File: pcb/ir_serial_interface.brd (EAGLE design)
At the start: 41.6 x 43.2 mm, 24 parts, among them IC1 PIC18F2550_28W, Q1 BSS123, T1 SFH303

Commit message: PCB: board layout done
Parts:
- removed GND, LEFT, MIC, RIGHT: LSP10, solpad:LSP10
- removed Q1: BSS123, transistor-small-signal:SOT23
- added D2: (no value), semicon-smd-ipc:SOT23
- added IC2: LP2992, texas:SOT23-DBV
- added Q2: BC847SMD, transistor-npn:SOT23
- added R10: 2k, resistor:M0805
- added R11, R12, R13: 100k, resistor:M0805
- added U$2: AUDIO-JACK3, SparkFun-Connectors:AUDIO-JACK-TRRS-SMD
- moved R3 23.3 mm to (53.3, 27.9), turned to 0 degrees
- moved C4 23.3 mm to (50.8, 47.0), turned to 0 degrees
- moved R9 19.1 mm to (25.4, 46.4), turned to 180 degrees
- moved C1 18.9 mm to (52.4, 30.8), turned to 0 degrees
- moved R4 17.6 mm to (48.9, 27.9), turned to 0 degrees
- moved U$1 17.4 mm to (42.5, 47.6)
- moved D4 16.7 mm to (24.1, 41.9), turned to 270 degrees
- moved T1 16.7 mm to (24.1, 34.3)
- moved R1 16.5 mm to (35.6, 47.6), turned to 0 degrees
- moved BAT1 15.9 mm to (46.4, 38.1)
- moved R2 15.3 mm to (25.4, 29.2), turned to 180 degrees
- moved D1 14.8 mm to (27.9, 41.9), turned to 270 degrees
- moved R8 11.0 mm to (29.8, 46.4), turned to 180 degrees
- moved R7 10.8 mm to (50.8, 43.8), turned to 180 degrees
- moved C2 7.62 mm to (44.5, 27.9), turned to 180 degrees
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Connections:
- removed net -: BAT1.2
- new net N$12: D2.1, U$2.RING1
- new net N$13: IC2.3, Q2.2, R11.1
- new net N$18: C4.1, D2.3, R10.2
- new net V+: BAT1.1, IC2.1, Q2.3, R13.2
- net +5V: now also IC2.5; no longer Q1.2
- net GND: now also BAT1.2, IC2.2, R11.2, R12.1, U$2.RING2; no longer GND.MP
- net N$16: now also IC1.7, R12.2, R13.1; no longer BAT1.1, Q1.3
- net N$17: now also Q2.1, R10.1; no longer C4.1, Q1.1, RIGHT.MP
- net N$5: now also U$2.TIP; no longer LEFT.MP
- net N$7: now also U$2.EARTH; no longer MIC.MP
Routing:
- net N$2: track 3.01 -> 0.00 mm
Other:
- board size 41.6 x 43.2 mm -> 41.6 x 25.4 mm

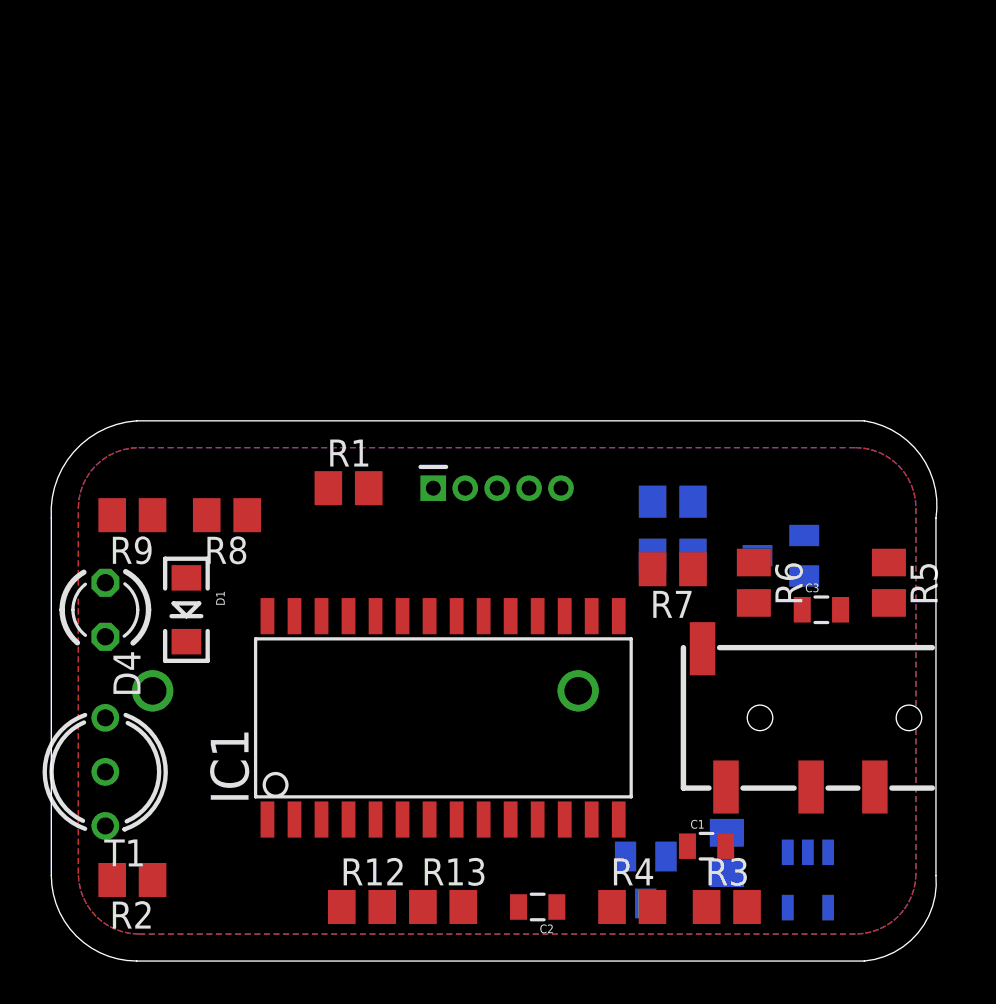
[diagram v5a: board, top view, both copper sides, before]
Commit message: PCB: routing done
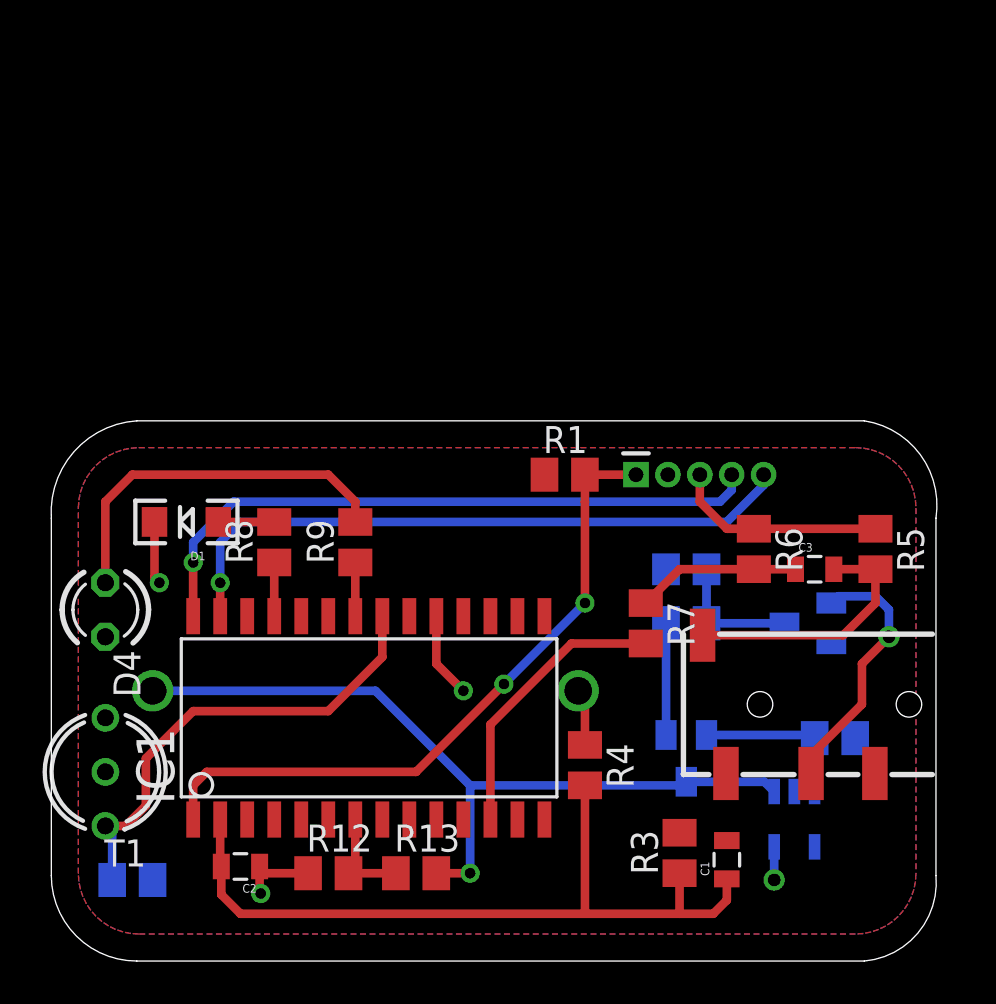
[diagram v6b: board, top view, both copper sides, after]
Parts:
- moved C2 14.1 mm to (30.5, 29.8)
- moved R9 10.6 mm to (35.9, 45.1), turned to 90 degrees
- moved R1 10.2 mm to (45.7, 48.3)
- moved U$1 9.55 mm to (52.1, 48.3)
- moved R11 7.41 mm to (58.4, 35.9), turned to 180 degrees
- moved R4 7.03 mm to (46.7, 34.6), turned to 270 degrees
- moved Q2 6.02 mm to (51.4, 34.9)
- moved D1 4.13 mm to (27.9, 46.0), turned to 180 degrees
- moved IC1 3.49 mm to (35.9, 36.8)
- moved D2 3.42 mm to (57.1, 41.3)
- moved R3 3.38 mm to (51.1, 30.5), turned to 90 degrees
- moved C4 3.24 mm to (51.4, 43.8)
- moved R10 3.24 mm to (51.4, 41.3)
- moved IC2 2.93 mm to (56.5, 32.1)
- moved R7 2.84 mm to (49.5, 41.3), turned to 270 degrees
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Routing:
- net V+: track 0.00 -> 37.0 mm, vias 0 -> 1
- net N$6: track 0.00 -> 36.9 mm
- net N$2: track 0.00 -> 32.0 mm, vias 0 -> 2
- net N$4: track 0.00 -> 30.6 mm, vias 0 -> 1
- net N$3: track 0.00 -> 30.5 mm, vias 0 -> 1
- net GND: track 0.00 -> 23.4 mm, vias 0 -> 3
- net N$1: track 0.00 -> 22.2 mm
- net N$14: track 0.00 -> 17.6 mm
- net N$9: track 0.00 -> 13.3 mm
- net N$12: track 0.00 -> 12.3 mm, vias 0 -> 1
- net N$7: track 0.00 -> 12.3 mm
- net N$8: track 0.00 -> 7.70 mm
- net N$13: track 0.00 -> 7.65 mm
- net N$18: track 0.00 -> 6.20 mm
- net N$17: track 0.00 -> 5.25 mm
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
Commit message: better space layout
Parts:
- moved R4 1.27 mm to (47.9, 34.6)
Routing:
- net GND: track 23.4 -> 23.9 mm
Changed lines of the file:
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@@
 <layers>
 <layer number="1" name="Top" color="4" fill="1" visible="yes" active="yes"/>
-<layer number="16" name="Bottom" color="1" fill="1" visible="yes" active="yes"/>
+<layer number="16" name="Bottom" color="1" fill="1" visible="no" active="yes"/>
 <layer number="17" name="Pads" color="2" fill="1" visible="yes" active="yes"/>
 <layer number="18" name="Vias" color="2" fill="1" visible="yes" active="yes"/>
@@
 <element name="D4" library="led" package="LED3MM" value="IR" x="24.13" y="41.91" rot="R270"/>
 <element name="C4" library="rcl" package="C0805" value="" x="51.435" y="43.815" rot="MR0"/>
-<element name="R4" library="resistor" package="M0805" value="100k" x="46.6725" y="34.6075" rot="R270"/>
+<element name="R4" library="resistor" package="M0805" value="100k" x="47.9425" y="34.6075" rot="R270"/>
 <element name="U$2" library="SparkFun-Connectors" package="AUDIO-JACK-TRRS-SMD" value="AUDIO-JACK3" x="63.5" y="37.465" rot="R180"/>
 <element name="Q2" library="transistor-npn" package="SOT23" value="BC847SMD" x="51.435" y="34.925" rot="MR180"/>
@@
 <contactref element="R11" pad="2"/>
 <contactref element="R12" pad="1"/>
-<wire x1="46.6725" y1="35.5575" x2="46.6725" y2="37.7825" width="0.4064" layer="1"/>
-<wire x1="46.6725" y1="37.7825" x2="46.355" y2="38.1" width="0.4064" layer="1"/>
 <wire x1="54.61" y1="45.7175" x2="60.325" y2="45.7175" width="0.4064" layer="1"/>
 <wire x1="54.61" y1="45.7175" x2="53.3425" y2="45.7175" width="0.4064" layer="1"/>
@@
 <wire x1="31.38" y1="28.6275" x2="31.4325" y2="28.575" width="0.4064" layer="1"/>
 <via x="31.4325" y="28.575" extent="1-16" drill="0.5"/>
+<wire x1="46.355" y1="38.1" x2="47.9425" y2="36.5125" width="0.4064" layer="1"/>
+<wire x1="47.9425" y1="36.5125" x2="47.9425" y2="35.5575" width="0.4064" layer="1"/>
 <wire x1="59.37" y1="35.8775" x2="60.3" y2="34.215" width="0" layer="19" extent="1-16"/>
 </signal>
@@
 <wire x1="29.58" y1="29.845" x2="29.58" y2="28.5225" width="0.4064" layer="1"/>
 <wire x1="29.58" y1="28.5225" x2="30.48" y2="27.6225" width="0.4064" layer="1"/>
-<wire x1="30.48" y1="27.6225" x2="46.6725" y2="27.6225" width="0.4064" layer="1"/>
-<wire x1="46.6725" y1="27.6225" x2="51.1175" y2="27.6225" width="0.4064" layer="1"/>
+<wire x1="30.48" y1="27.6225" x2="47.9425" y2="27.6225" width="0.4064" layer="1"/>
+<wire x1="47.9425" y1="27.6225" x2="51.1175" y2="27.6225" width="0.4064" layer="1"/>
 <wire x1="51.1175" y1="27.6225" x2="52.705" y2="27.6225" width="0.4064" layer="1"/>
 <wire x1="52.705" y1="27.6225" x2="53.34" y2="28.2575" width="0.4064" layer="1"/>
 <wire x1="53.34" y1="28.2575" x2="53.34" y2="29.2625" width="0.4064" layer="1"/>
 <wire x1="51.1175" y1="29.53" x2="51.1175" y2="27.6225" width="0.4064" layer="1"/>
-<wire x1="46.6725" y1="33.6575" x2="46.6725" y2="27.6225" width="0.4064" layer="1"/>
+<wire x1="47.9425" y1="33.6575" x2="47.9425" y2="27.6225" width="0.4064" layer="1"/>
 </signal>
 <signal name="N$7">

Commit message: silk screen cleanup
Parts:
- removed D4: IR, led:LED3MM
- added D3: (no value), semicon-smd-ipc:SOT23
- D1: value RED -> IR; device SparkFun-LED:LED-1206 -> led:LED3MM
- D2: value (none) -> RED; device semicon-smd-ipc:SOT23 -> SparkFun-LED:LED-1206
- moved D2 29.6 mm to (27.9, 46.0), flipped to the top, turned to 180 degrees
- moved D1 5.62 mm to (24.1, 41.9), turned to 270 degrees
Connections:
- net GND: now also D1.K, D2.C; no longer D1.C, D4.K
- net N$10: now also D2.A; no longer D1.A
- net N$12: now also D3.1; no longer D2.1
- net N$14: now also D1.A; no longer D4.A
- net N$18: now also D3.3; no longer D2.3
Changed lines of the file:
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@@
 </autorouter>
 <elements>
-<element name="T1" library="opto-trans-siemens" package="SFH303" value="SFH303" x="24.13" y="34.29" rot="R180">
+<element name="T1" library="opto-trans-siemens" package="SFH303" value="SFH303" x="24.13" y="34.29" smashed="yes" rot="R180">
 <attribute name="OC_NEWARK" value="unknown" x="24.13" y="34.29" size="1.778" layer="27" rot="R180" display="off"/>
 <attribute name="MPN" value="" x="24.13" y="34.29" size="1.778" layer="27" rot="R180" display="off"/>
 <attribute name="MF" value="" x="24.13" y="34.29" size="1.778" layer="27" rot="R180" display="off"/>
 <attribute name="OC_FARNELL" value="unknown" x="24.13" y="34.29" size="1.778" layer="27" rot="R180" display="off"/>
+<attribute name="NAME" x="25.4" y="35.2425" size="1.016" layer="25" ratio="10" rot="R270"/>
 </element>
 <element name="R2" library="resistor" package="M0805" value="10k" x="25.4" y="29.21" rot="MR0"/>
@@
 <element name="R3" library="resistor" package="M0805" value="100k" x="51.1175" y="30.48" rot="R90"/>
 <element name="C1" library="SparkFun (old)" package="0805" value="0.2uF" x="53.34" y="30.1625" rot="R90"/>
-<element name="IC1" library="microchip" package="SO28W" value="PIC18F2550_28W" x="35.8775" y="36.83">
+<element name="IC1" library="microchip" package="SO28W" value="PIC18F2550_28W" x="35.8775" y="36.83" smashed="yes">
 <attribute name="OC_NEWARK" value="73K1297" x="35.8775" y="36.83" size="1.778" layer="27" display="off"/>
 <attribute name="MPN" value="PIC18F2550-I/SO" x="35.8775" y="36.83" size="1.778" layer="27" display="off"/>
 <attribute name="MF" value="MICROCHIP" x="35.8775" y="36.83" size="1.778" layer="27" display="off"/>
 <attribute name="OC_FARNELL" value="9321268" x="35.8775" y="36.83" size="1.778" layer="27" display="off"/>
+<attribute name="NAME" x="27.686" y="34.9885" size="1.016" layer="25" ratio="10" rot="R90"/>
+<attribute name="VALUE" x="45.339" y="43.6245" size="0.6096" layer="27" ratio="10" rot="R180"/>
 </element>
 <element name="C2" library="SparkFun (old)" package="0805" value="47pF" x="30.48" y="29.845" rot="R180"/>
@@
 <element name="R6" library="resistor" package="M0805" value="2k" x="54.61" y="44.7675" rot="R270"/>
 <element name="R7" library="resistor" package="M0805" value="10k" x="49.53" y="41.275" rot="R270"/>
-<element name="D1" library="SparkFun-LED" package="LED-1206" value="RED" x="27.94" y="46.0375" rot="R180">
+<element name="D2" library="SparkFun-LED" package="LED-1206" value="RED" x="27.94" y="46.0375" smashed="yes" rot="R180">
 <attribute name="PROD_ID" value="DIO-09912" x="27.94" y="46.0375" size="1.778" layer="27" rot="R180" display="off"/>
+<attribute name="NAME" x="28.829" y="48.4505" size="1.016" layer="25" ratio="10" rot="R180"/>
 </element>
 <element name="R8" library="resistor" package="M0805" value="190" x="32.0675" y="45.085" rot="R90"/>
 <element name="BAT1" library="SparkFun-Electromechanical" package="BATTCOM_20MM_PTH" value="20mm coincell" x="46.355" y="38.1" rot="MR0"/>
 <element name="R9" library="resistor" package="M0805" value="190" x="35.8775" y="45.085" rot="R90"/>
-<element name="D4" library="led" package="LED3MM" value="IR" x="24.13" y="41.91" rot="R270"/>
+<element name="D1" library="led" package="LED3MM" value="IR" x="24.13" y="41.91" smashed="yes" rot="R270">
+<attribute name="NAME" x="26.0985" y="41.91" size="1.016" layer="25" ratio="10" rot="R270"/>
+</element>
 <element name="C4" library="rcl" package="C0805" value="" x="51.435" y="43.815" rot="MR0"/>
 <element name="R4" library="resistor" package="M0805" value="100k" x="47.9425" y="34.6075" rot="R270"/>
 <element name="U$2" library="SparkFun-Connectors" package="AUDIO-JACK-TRRS-SMD" value="AUDIO-JACK3" x="63.5" y="37.465" rot="R180"/>
 <element name="Q2" library="transistor-npn" package="SOT23" value="BC847SMD" x="51.435" y="34.925" rot="MR180"/>
-<element name="D2" library="semicon-smd-ipc" package="SOT23" value="" x="57.15" y="41.275" rot="MR270"/>
+<element name="D3" library="semicon-smd-ipc" package="SOT23" value="" x="57.15" y="41.275" smashed="yes" rot="MR270">
+<attribute name="NAME" x="56.1975" y="43.815" size="0.6096" layer="26" rot="MR180"/>
+<attribute name="VALUE" x="60.325" y="43.18" size="1.27" layer="28" rot="MR270"/>
+</element>
 <element name="R10" library="resistor" package="M0805" value="2k" x="51.435" y="41.275" rot="MR180"/>
-<element name="IC2" library="texas" package="SOT23-DBV" value="LP2992" x="56.515" y="32.0675" rot="MR180">
+<element name="IC2" library="texas" package="SOT23-DBV" value="LP2992" x="56.515" y="32.0675" smashed="yes" rot="MR180">
 <attribute name="OC_NEWARK" value="77C1171" x="56.515" y="32.0675" size="1.778" layer="28" rot="MR180" display="off"/>
 <attribute name="MPN" value="TPS77001DBVT" x="56.515" y="32.0675" size="1.778" layer="28" rot="MR180" display="off"/>
 <attribute name="MF" value="TEXAS INSTRUMENTS" x="56.515" y="32.0675" size="1.778" layer="28" rot="MR180" display="off"/>
 <attribute name="OC_FARNELL" value="8461554" x="56.515" y="32.0675" size="1.778" layer="28" rot="MR180" display="off"/>
+<attribute name="NAME" x="58.7375" y="33.02" size="0.6096" layer="26" rot="MR270"/>
+<attribute name="VALUE" x="54.0385" y="30.48" size="0.6096" layer="28" rot="MR90"/>
 </element>
 <element name="R11" library="resistor" package="M0805" value="100k" x="58.42" y="35.8775" rot="MR180"/>
@@
 <contactref element="R5" pad="1"/>
 <contactref element="R6" pad="1"/>
-<contactref element="D1" pad="C"/>
-<contactref element="D4" pad="K"/>
+<contactref element="D2" pad="C"/>
+<contactref element="D1" pad="K"/>
 <contactref element="R4" pad="1"/>
 <contactref element="U$2" pad="RING2"/>
@@
 </signal>
 <signal name="N$10">
-<contactref element="D1" pad="A"/>
+<contactref element="D2" pad="A"/>
 <contactref element="R8" pad="2"/>
 <wire x1="32.0675" y1="46.035" x2="29.4425" y2="46.035" width="0.4064" layer="1"/>
@@
 </signal>
 <signal name="N$14">
-<contactref element="D4" pad="A"/>
+<contactref element="D1" pad="A"/>
 <contactref element="R9" pad="2"/>
 <wire x1="24.13" y1="43.18" x2="24.13" y2="46.99" width="0.4064" layer="1"/>
@@
 </signal>
 <signal name="N$12">
-<contactref element="D2" pad="1"/>
+<contactref element="D3" pad="1"/>
 <contactref element="U$2" pad="RING1"/>
 <wire x1="57.3" y1="34.215" x2="57.3" y2="35.075" width="0.4064" layer="1"/>
@@
 </signal>
 <signal name="N$18">
-<contactref element="D2" pad="3"/>
+<contactref element="D3" pad="3"/>
 <contactref element="R10" pad="2"/>
 <contactref element="C4" pad="1"/>
